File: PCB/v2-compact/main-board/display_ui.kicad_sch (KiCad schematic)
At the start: 0 parts

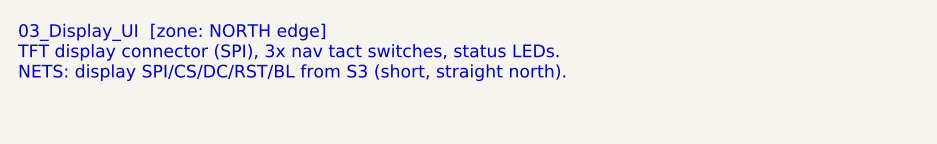
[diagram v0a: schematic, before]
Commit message: PCB: rework main board to phone-style layout; J1 -> horizontal strip
Main board (per feedback) is now a phone-style split — front is pure UI, back
carries the electronics:
- FRONT: status LEDs at the very top (above the display), TFT rotated to
  LANDSCAPE (sideways), nav buttons below it and moved down. Same feel as the
  ESP32-DIV, sideways screen.
- BACK: ESP32-S3 behind the display, microSD beside it, power + USB-C at the
  bottom-centre edge like a phone.

To keep the centre column free for the landscape display and the bottom-centre
USB-C, J1 is reoriented from a vertical 2x10 to a HORIZONTAL 10x2 strip in the
lower-centre. J1 is the shared mating datum, so the shield's J1 moves to match;
the shield's RV1106 / HTRC110 / bulk-cap zones shift to sit above/below the new
strip (SPI spine still runs north from it). Every v1 capability unchanged.

Updated both .kicad_pcb, both floorplan SVGs, both schematics' zone specs, and
PLACEMENT.md. Verified: files parse, J1 clears all zones, no same-side overlaps.

Co-Authored-By: Claude <noreply@anthropic.com>
Claude-Session: https://claude.ai/code/session_017BEAKBRVwbUCc7Sa2o3Ye7
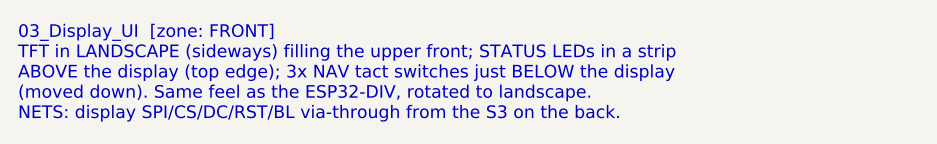
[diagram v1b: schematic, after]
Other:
- note added: "03_Display_UI [zone: FRONT] TFT in LANDSCAPE (sideways) filling the upper front; STATUS LEDs in a strip ABOVE the display (top edge); 3x NAV tact switches just BELOW the display (moved down). Same feel as the ESP32-DIV, rotated to landscape. NETS: display SPI/CS/DC/RST/BL via-through from the S3 on the back."
- note removed: "03_Display_UI [zone: NORTH edge] TFT display connector (SPI), 3x nav tact switches, status LEDs. NETS: display SPI/CS/DC/RST/BL from S3 (short, straight north)."
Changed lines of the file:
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@@
   (paper "A4")
   (title_block (title "03_Display_UI") (company "YurilLAB"))
-  (text "03_Display_UI  [zone: NORTH edge]
-TFT display connector (SPI), 3x nav tact switches, status LEDs.
-NETS: display SPI/CS/DC/RST/BL from S3 (short, straight north)." (at 15 15 0)
+  (text "03_Display_UI  [zone: FRONT]
+TFT in LANDSCAPE (sideways) filling the upper front; STATUS LEDs in a strip
+ABOVE the display (top edge); 3x NAV tact switches just BELOW the display
+(moved down). Same feel as the ESP32-DIV, rotated to landscape.
+NETS: display SPI/CS/DC/RST/BL via-through from the S3 on the back." (at 15 15 0)
     (effects (font (size 1.4 1.4)) (justify left top)))
   (sheet_instances (path "/" (page "1")))
